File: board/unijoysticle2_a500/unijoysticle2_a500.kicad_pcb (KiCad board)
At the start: 4 copper layers, 67 x 52 mm, 54 parts, among them J1 USB_B_Micro, J2 PORT JOY #1, J3 PORT JOY #2, Q1 S8050, Q2 S8050, SW1 RESET, SW2 BOOT, SW3 MOUSE, SW4 SWAP, U1 ESP32-WROOM-32E, U2 AMS1117-3.3, U3 CH340C, U4 74HC05, U5 74HC05, U6 74HC05

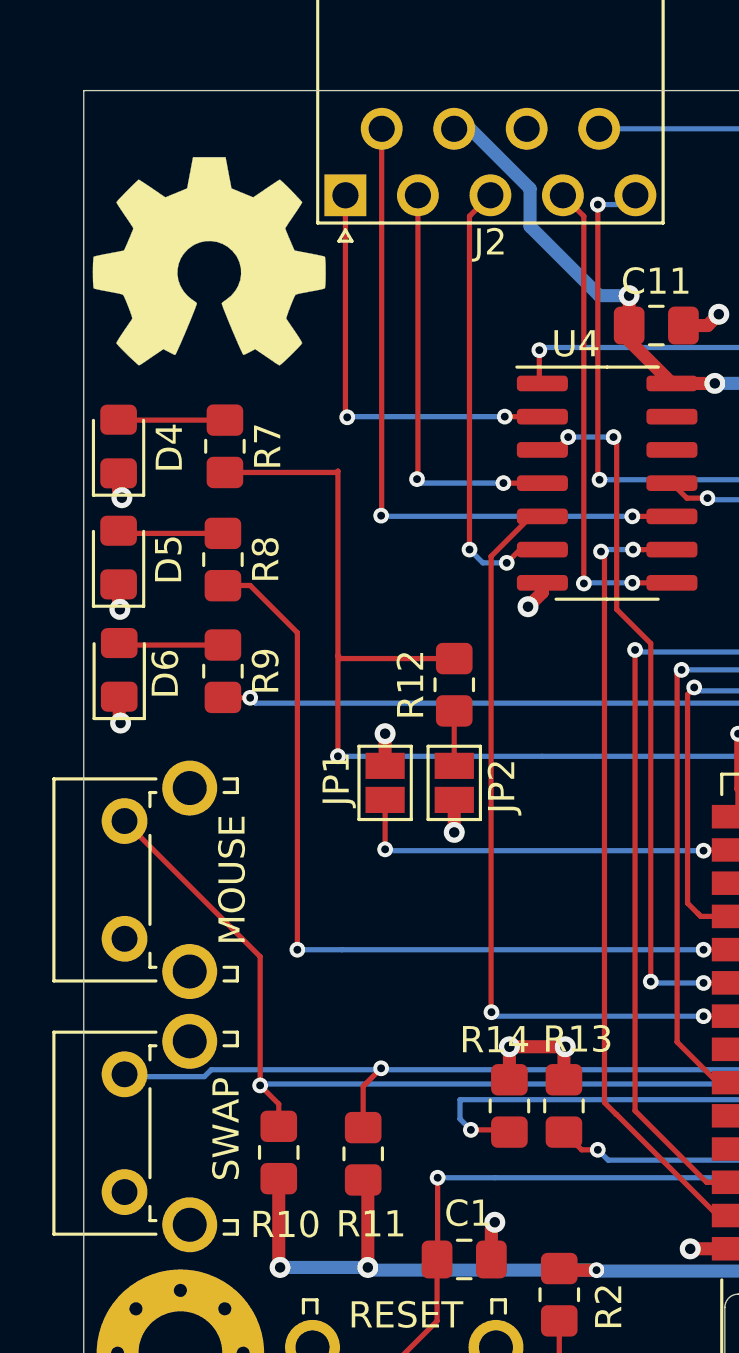
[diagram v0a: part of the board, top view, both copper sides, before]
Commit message: a500: layout with open hardware logo in copper
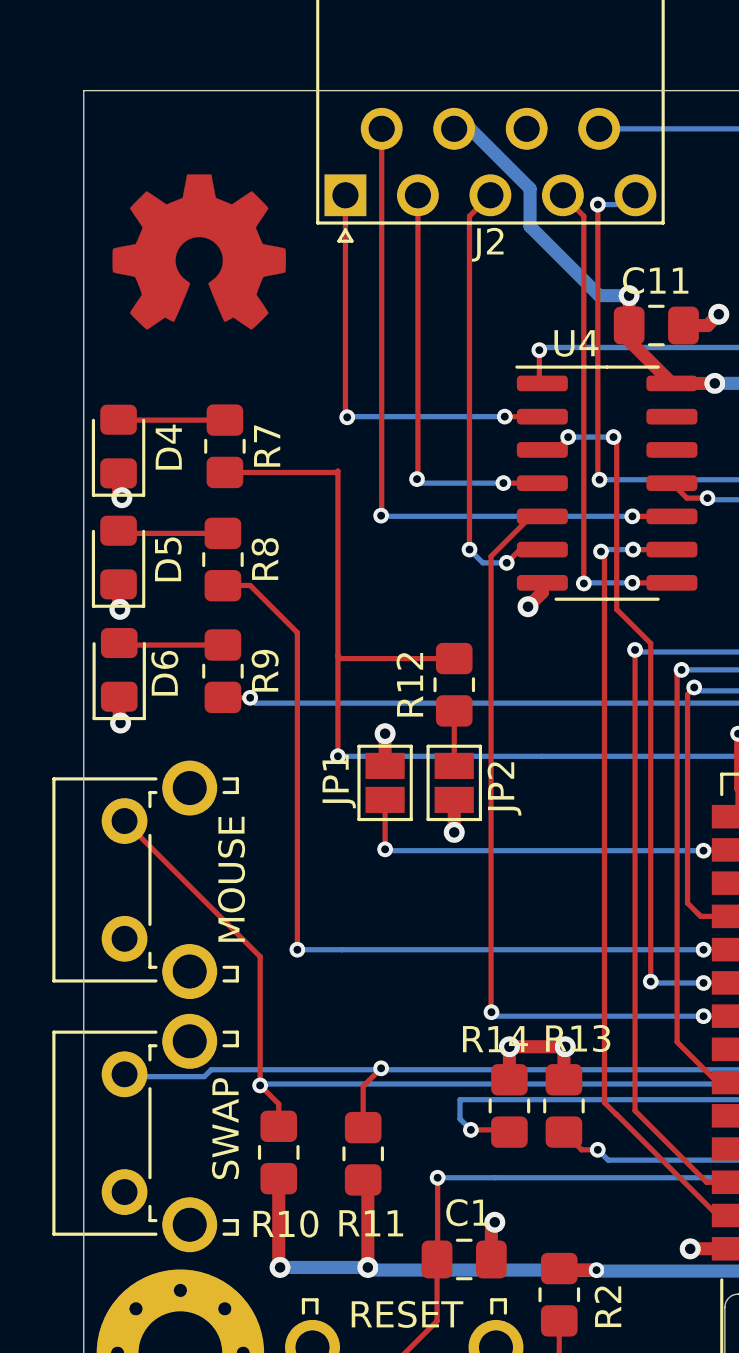
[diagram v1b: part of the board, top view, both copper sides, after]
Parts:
- removed the REF** at (84.8, 102.5)
- added REF**: OSHW-Symbol_6.7x6mm_Copper, Symbol:OSHW-Symbol_6.7x6mm_Copper, F.Cu at (84.4, 102.2)

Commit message: uni a500: add JV
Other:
- board text added: "J"
- board text added: "V"
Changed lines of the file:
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@@
       (drillshape 0)
       (scaleselection 1)
-      (outputdirectory "gerber_a/")
+      (outputdirectory "assembly_a/")
     )
   )
@@
   (gr_line (start 128.5 147) (end 128 148) (layer "Edge.Cuts") (width 0.05))
   (gr_line (start 121.99259 141.98961) (end 105.00721 141.98961) (layer "Edge.Cuts") (width 0.05))
+  (gr_text "V" (at 92.2528 145.6) (layer "B.Cu")
+    (effects (font (size 1.5 1.5) (thickness 0.3)))
+  )
+  (gr_text "J" (at 132.3848 145.6) (layer "B.Cu")
+    (effects (font (size 1.5 1.5) (thickness 0.3)) (justify mirror))
+  )
   (gr_text "Unijoysticle 2 A500\nRev. A" (at 113.62 131.185) (layer "B.SilkS")
     (effects (font (size 1.5 1.5) (thickness 0.3)) (justify mirror))

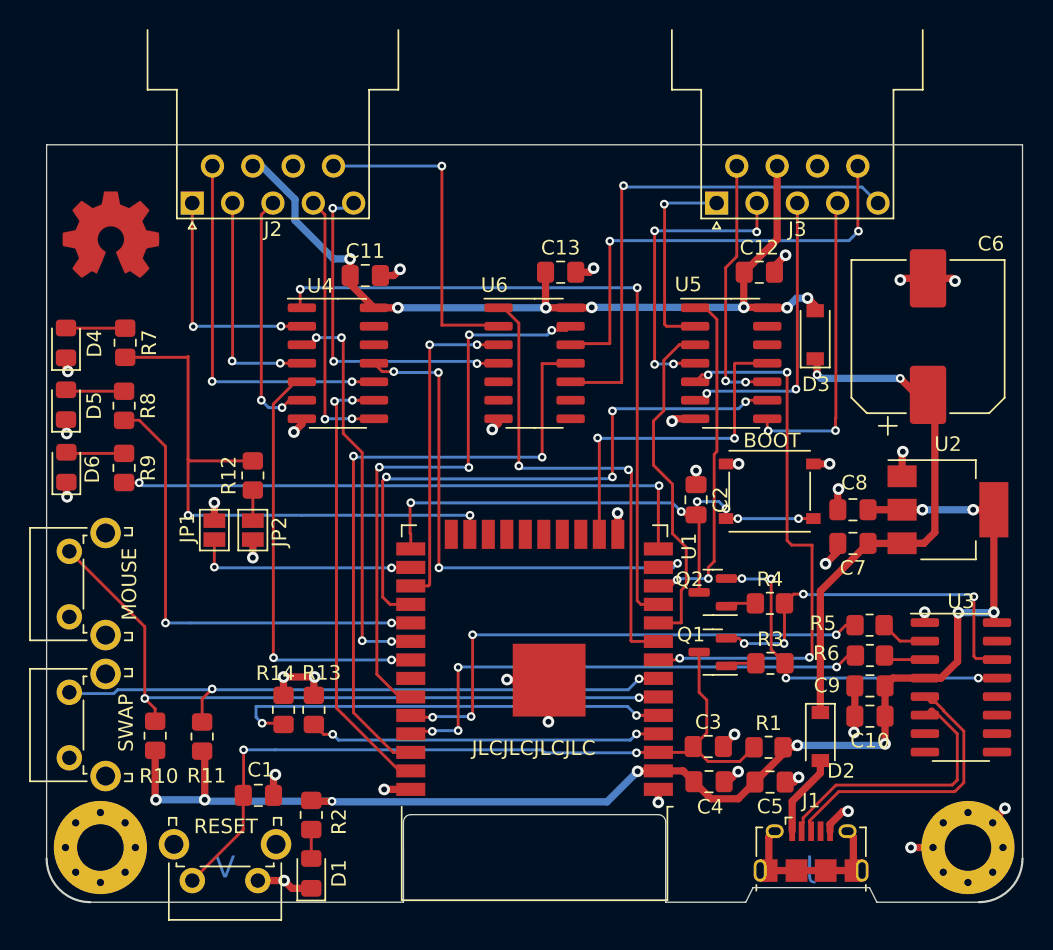
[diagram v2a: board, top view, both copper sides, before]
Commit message: uni2 a500: vias closer to pads
And also improved routing of some of the wires... shorter path
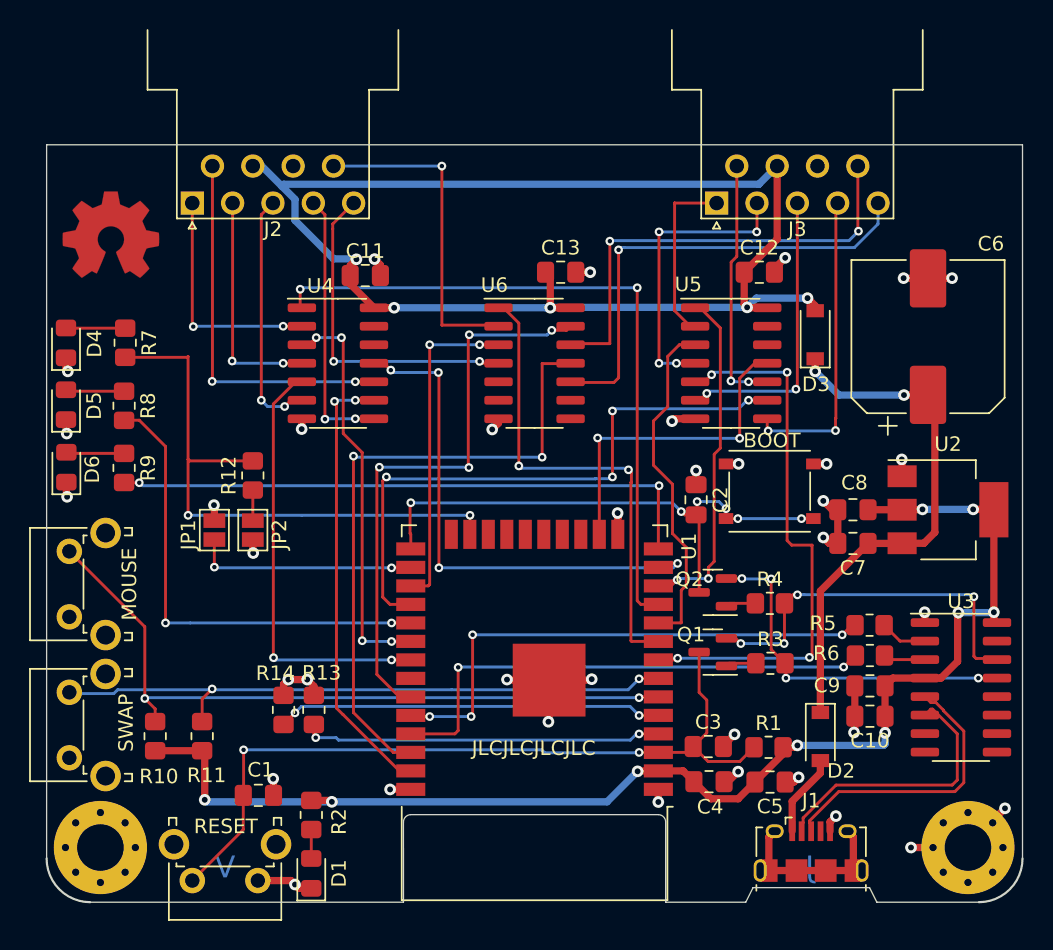
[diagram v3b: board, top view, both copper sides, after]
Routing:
- net +5V: track 58.7 -> 97.2 mm, vias 7 -> 5
- net GPIO_39: track 30.7 -> 26.5 mm
- net +3V3: track 93.9 -> 90.6 mm, vias 10 -> 9
- net /Amiga Ports/J2_POTY: track 35.1 -> 32.2 mm
- net /Amiga Ports/J2_UP: track 14.0 -> 12.1 mm, vias 1 -> 0
- net /Amiga Ports/J2_DOWN: track 21.0 -> 20.2 mm
- net /Amiga Ports/J1_LEFT: track 17.1 -> 17.9 mm
- net GPIO_J2_UP: track 24.3 -> 23.5 mm
- net /Amiga Ports/J1_POTY: track 23.5 -> 22.9 mm, vias 3 -> 2
- net GPIO_J2_FIRE: track 23.4 -> 22.9 mm
- net /Amiga Ports/J2_FIRE: track 18.0 -> 17.4 mm
- net GND: track 60.0 -> 59.8 mm, vias 36 -> 37
- net UART_RX: vias 4 -> 2

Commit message: uni a500+: remove LSCS column
Values were outdated
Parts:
- R1, R3, R4: value 10k -> 10K
- R5, R6: value 1k -> 1K

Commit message: uni a500: add no-connect to 74HC05 pin
In the schematic, add the no-connect to the pins that are not used.
Fixes some warnings
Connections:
- U4 pad 12: (no net) -> unconnected-(U4-Pad12)
- U4 pad 13: (no net) -> unconnected-(U4-Pad13)
- U5 pad 12: (no net) -> unconnected-(U5-Pad12)
- U5 pad 13: (no net) -> unconnected-(U5-Pad13)
- U6 pad 5: (no net) -> unconnected-(U6-Pad5)
- U6 pad 6: (no net) -> unconnected-(U6-Pad6)
- U6 pad 8: (no net) -> unconnected-(U6-Pad8)
- U6 pad 9: (no net) -> unconnected-(U6-Pad9)
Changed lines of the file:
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@@
   (net 74 "GPIO_36")
   (net 75 "Net-(JP2-Pad2)")
+  (net 76 "unconnected-(U4-Pad12)")
+  (net 77 "unconnected-(U4-Pad13)")
+  (net 78 "unconnected-(U5-Pad12)")
+  (net 79 "unconnected-(U5-Pad13)")
+  (net 80 "unconnected-(U6-Pad5)")
+  (net 81 "unconnected-(U6-Pad6)")
+  (net 82 "unconnected-(U6-Pad8)")
+  (net 83 "unconnected-(U6-Pad9)")
   (footprint "Connector_USB:USB_Micro-B_Amphenol_10118194_Horizontal" (layer "F.Cu")
     (at 132.4864 144.526)
@@
     (pad "11" smd roundrect (at 2.475 0) (size 1.95 0.6) (layers "F.Cu" "F.Paste" "F.Mask") (roundrect_rratio 0.25)
       (net 28 "GPIO_J1_FIRE") (pintype "input"))
-    (pad "12" smd roundrect (at 2.475 -1.27) (size 1.95 0.6) (layers "F.Cu" "F.Paste" "F.Mask") (roundrect_rratio 0.25))
-    (pad "13" smd roundrect (at 2.475 -2.54) (size 1.95 0.6) (layers "F.Cu" "F.Paste" "F.Mask") (roundrect_rratio 0.25))
+    (pad "12" smd roundrect (at 2.475 -1.27) (size 1.95 0.6) (layers "F.Cu" "F.Paste" "F.Mask") (roundrect_rratio 0.25)
+      (net 76 "unconnected-(U4-Pad12)") (pintype "open_collector+no_connect"))
+    (pad "13" smd roundrect (at 2.475 -2.54) (size 1.95 0.6) (layers "F.Cu" "F.Paste" "F.Mask") (roundrect_rratio 0.25)
+      (net 77 "unconnected-(U4-Pad13)") (pintype "input+no_connect"))
     (pad "14" smd roundrect (at 2.475 -3.81) (size 1.95 0.6) (layers "F.Cu" "F.Paste" "F.Mask") (roundrect_rratio 0.25)
       (net 15 "+5V") (pinfunction "VCC") (pintype "power_in"))
@@
     (pad "4" smd roundrect (at -2.475 0) (size 1.95 0.6) (layers "F.Cu" "F.Paste" "F.Mask") (roundrect_rratio 0.25)
       (net 44 "/Amiga Ports/J1_POTY") (pintype "open_collector"))
-    (pad "5" smd roundrect (at -2.475 1.27) (size 1.95 0.6) (layers "F.Cu" "F.Paste" "F.Mask") (roundrect_rratio 0.25))
-    (pad "6" smd roundrect (at -2.475 2.54) (size 1.95 0.6) (layers "F.Cu" "F.Paste" "F.Mask") (roundrect_rratio 0.25))
+    (pad "5" smd roundrect (at -2.475 1.27) (size 1.95 0.6) (layers "F.Cu" "F.Paste" "F.Mask") (roundrect_rratio 0.25)
+      (net 80 "unconnected-(U6-Pad5)") (pintype "input+no_connect"))
+    (pad "6" smd roundrect (at -2.475 2.54) (size 1.95 0.6) (layers "F.Cu" "F.Paste" "F.Mask") (roundrect_rratio 0.25)
+      (net 81 "unconnected-(U6-Pad6)") (pintype "open_collector+no_connect"))
     (pad "7" smd roundrect (at -2.475 3.81) (size 1.95 0.6) (layers "F.Cu" "F.Paste" "F.Mask") (roundrect_rratio 0.25)
       (net 72 "GND") (pinfunction "GND") (pintype "power_in"))
-    (pad "8" smd roundrect (at 2.475 3.81) (size 1.95 0.6) (layers "F.Cu" "F.Paste" "F.Mask") (roundrect_rratio 0.25))
-    (pad "9" smd roundrect (at 2.475 2.54) (size 1.95 0.6) (layers "F.Cu" "F.Paste" "F.Mask") (roundrect_rratio 0.25))
+    (pad "8" smd roundrect (at 2.475 3.81) (size 1.95 0.6) (layers "F.Cu" "F.Paste" "F.Mask") (roundrect_rratio 0.25)
+      (net 82 "unconnected-(U6-Pad8)") (pintype "open_collector+no_connect"))
+    (pad "9" smd roundrect (at 2.475 2.54) (size 1.95 0.6) (layers "F.Cu" "F.Paste" "F.Mask") (roundrect_rratio 0.25)
+      (net 83 "unconnected-(U6-Pad9)") (pintype "input+no_connect"))
     (pad "10" smd roundrect (at 2.475 1.27) (size 1.95 0.6) (layers "F.Cu" "F.Paste" "F.Mask") (roundrect_rratio 0.25)
       (net 51 "/Amiga Ports/J2_POTY") (pintype "open_collector"))
@@
     (pad "11" smd roundrect (at 2.475 0) (size 1.95 0.6) (layers "F.Cu" "F.Paste" "F.Mask") (roundrect_rratio 0.25)
       (net 30 "GPIO_J2_FIRE") (pintype "input"))
-    (pad "12" smd roundrect (at 2.475 -1.27) (size 1.95 0.6) (layers "F.Cu" "F.Paste" "F.Mask") (roundrect_rratio 0.25))
-    (pad "13" smd roundrect (at 2.475 -2.54) (size 1.95 0.6) (layers "F.Cu" "F.Paste" "F.Mask") (roundrect_rratio 0.25))
+    (pad "12" smd roundrect (at 2.475 -1.27) (size 1.95 0.6) (layers "F.Cu" "F.Paste" "F.Mask") (roundrect_rratio 0.25)
+      (net 78 "unconnected-(U5-Pad12)") (pintype "open_collector+no_connect"))
+    (pad "13" smd roundrect (at 2.475 -2.54) (size 1.95 0.6) (layers "F.Cu" "F.Paste" "F.Mask") (roundrect_rratio 0.25)
+      (net 79 "unconnected-(U5-Pad13)") (pintype "input+no_connect"))
     (pad "14" smd roundrect (at 2.475 -3.81) (size 1.95 0.6) (layers "F.Cu" "F.Paste" "F.Mask") (roundrect_rratio 0.25)
       (net 15 "+5V") (pinfunction "VCC") (pintype "power_in"))
